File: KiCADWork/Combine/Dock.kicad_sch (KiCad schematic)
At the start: 18 parts, among them J1 Conn_01x10_Socket, J1 USB_C_Receptacle, P1 USB_C_Plug, P2 USB_C_Plug

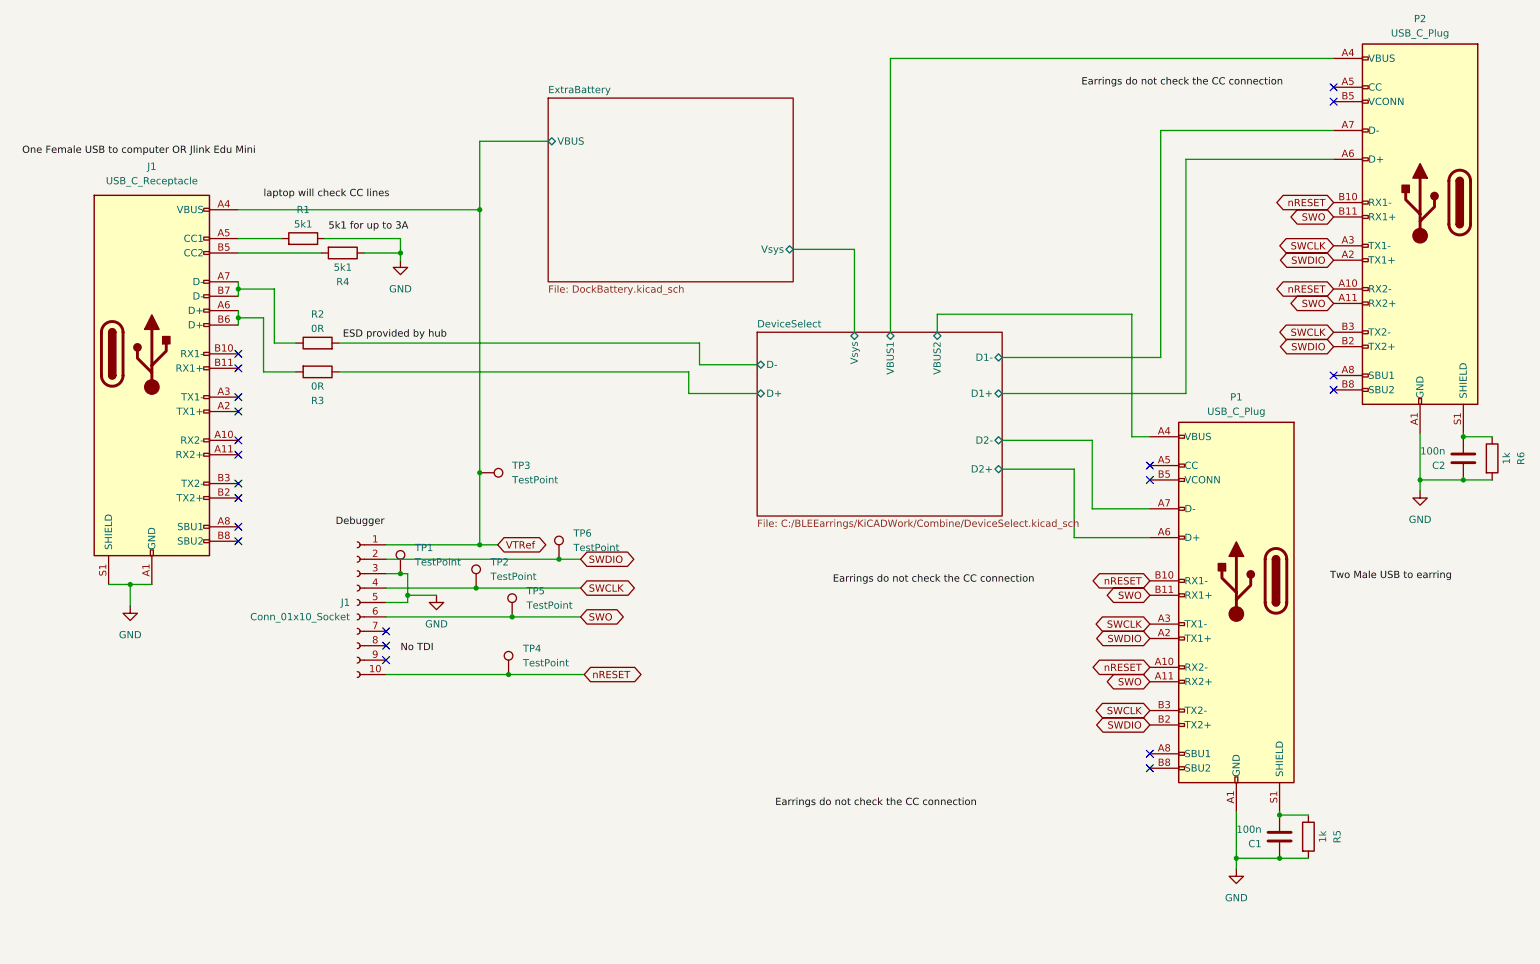
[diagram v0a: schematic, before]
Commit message: Completing the combined layout
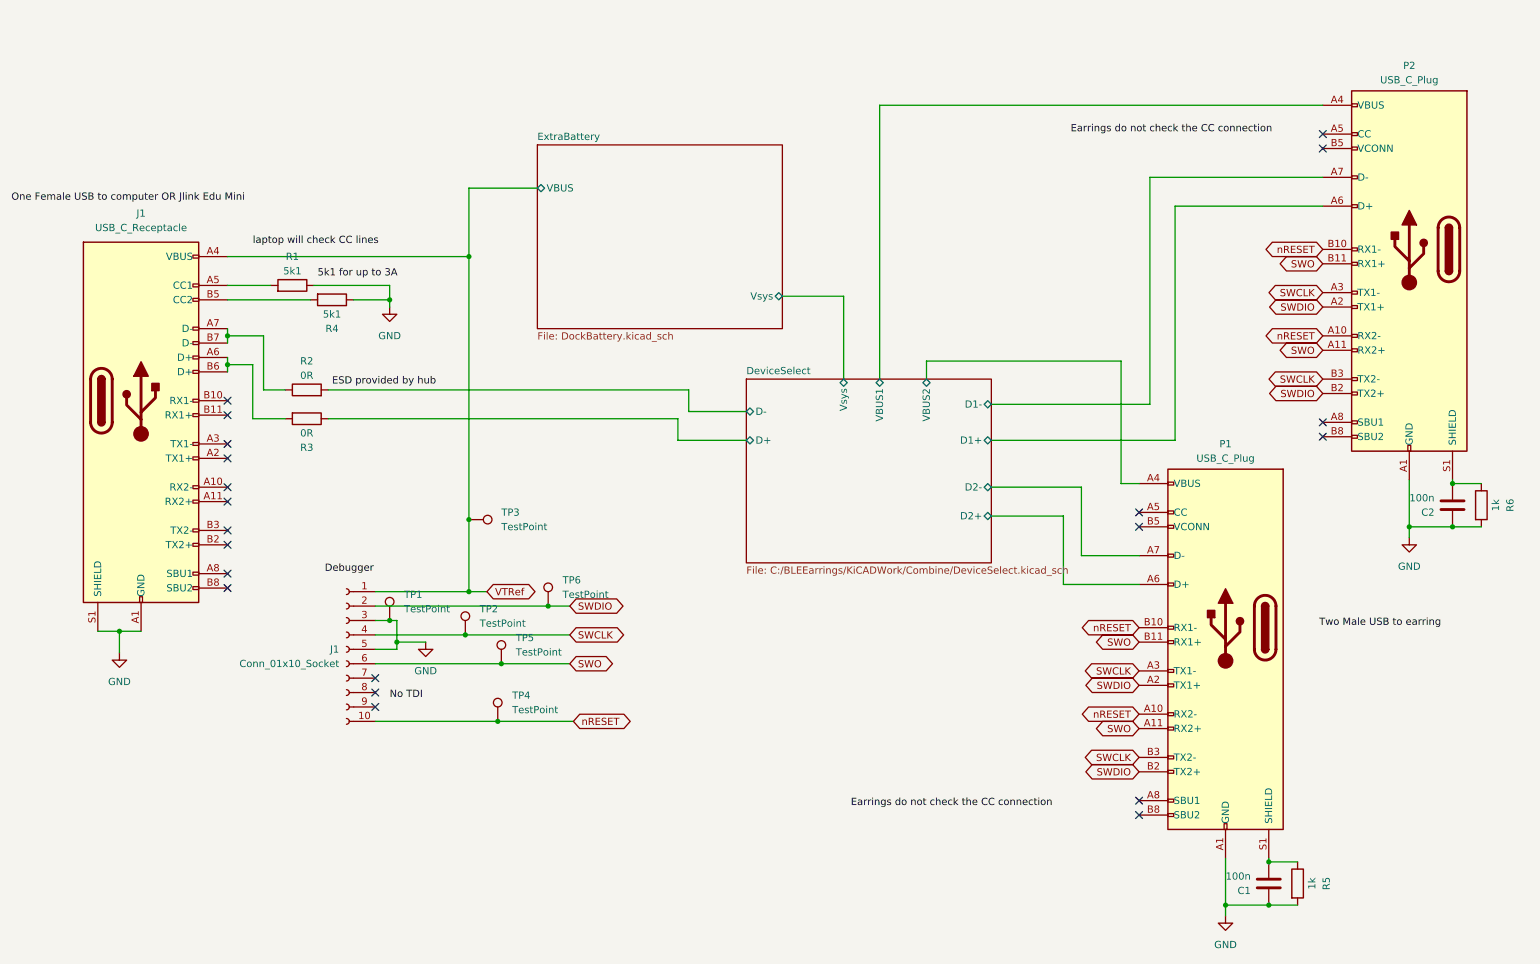
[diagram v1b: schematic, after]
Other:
- moved on the sheet: C1, C2, J1, P1, P2, R1, R2, R3, R4, R5, R6, TP1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

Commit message: Schem rev 1 pt1
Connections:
- net VTRef: no longer J1.1 (Pin_1), J1.A4 (VBUS), J1.A9 (VBUS), J1.B4 (VBUS), J1.B9 (VBUS), TP3.1
- new net +3V3: J1.1 (Pin_1)
- new net ExtraBattery/VBUS: J1.A4 (VBUS), J1.A9 (VBUS), J1.B4 (VBUS), J1.B9 (VBUS), TP3.1
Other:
- moved on the sheet: J1, R1, R2, R3, R4, TP3
